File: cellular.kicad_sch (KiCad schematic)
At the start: 50 parts, among them J301 Conn_Coaxial, J302 Conn_Coaxial, J304 SIM8060-6-1-14-00-A, Q301 MMBT3904, Q302 MMBT3904, U301 BG95-M3, U302 SN74AXC4T245QPWRQ1, U303 SN74AXC4T245QPWRQ1

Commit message: hierarchy
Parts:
- renumbered C315 to C70, C325 to C71, C316 to C72, C326 to C73, C304 to C74, C305 to C75, C320 to C76, C301 to C77, C319 to C78, C318 to C79, C306 to C80, C302 to C81, C317 to C82, C307 to C83, C303 to C84, C308 to C85, C309 to C86, C310 to C87, D305 to D5, D304 to D6, D303 to D7, D302 to D8, FB301 to FB1, J304 to J5, J301 to J6, J302 to J7, Q302 to Q6, Q301 to Q7, R305 to R59, R303 to R60, R306 to R61, R304 to R62, R309 to R63, R310 to R64, R308 to R65, R312 to R66, R302 to R67, R311 to R68, R301 to R69, TP302 to TP18, TP303 to TP19, TP304 to TP20, TP305 to TP21, TP306 to TP22, TP307 to TP23, TP308 to TP24, TP301 to TP25, U302 to U24, U303 to U25, U301 to U26

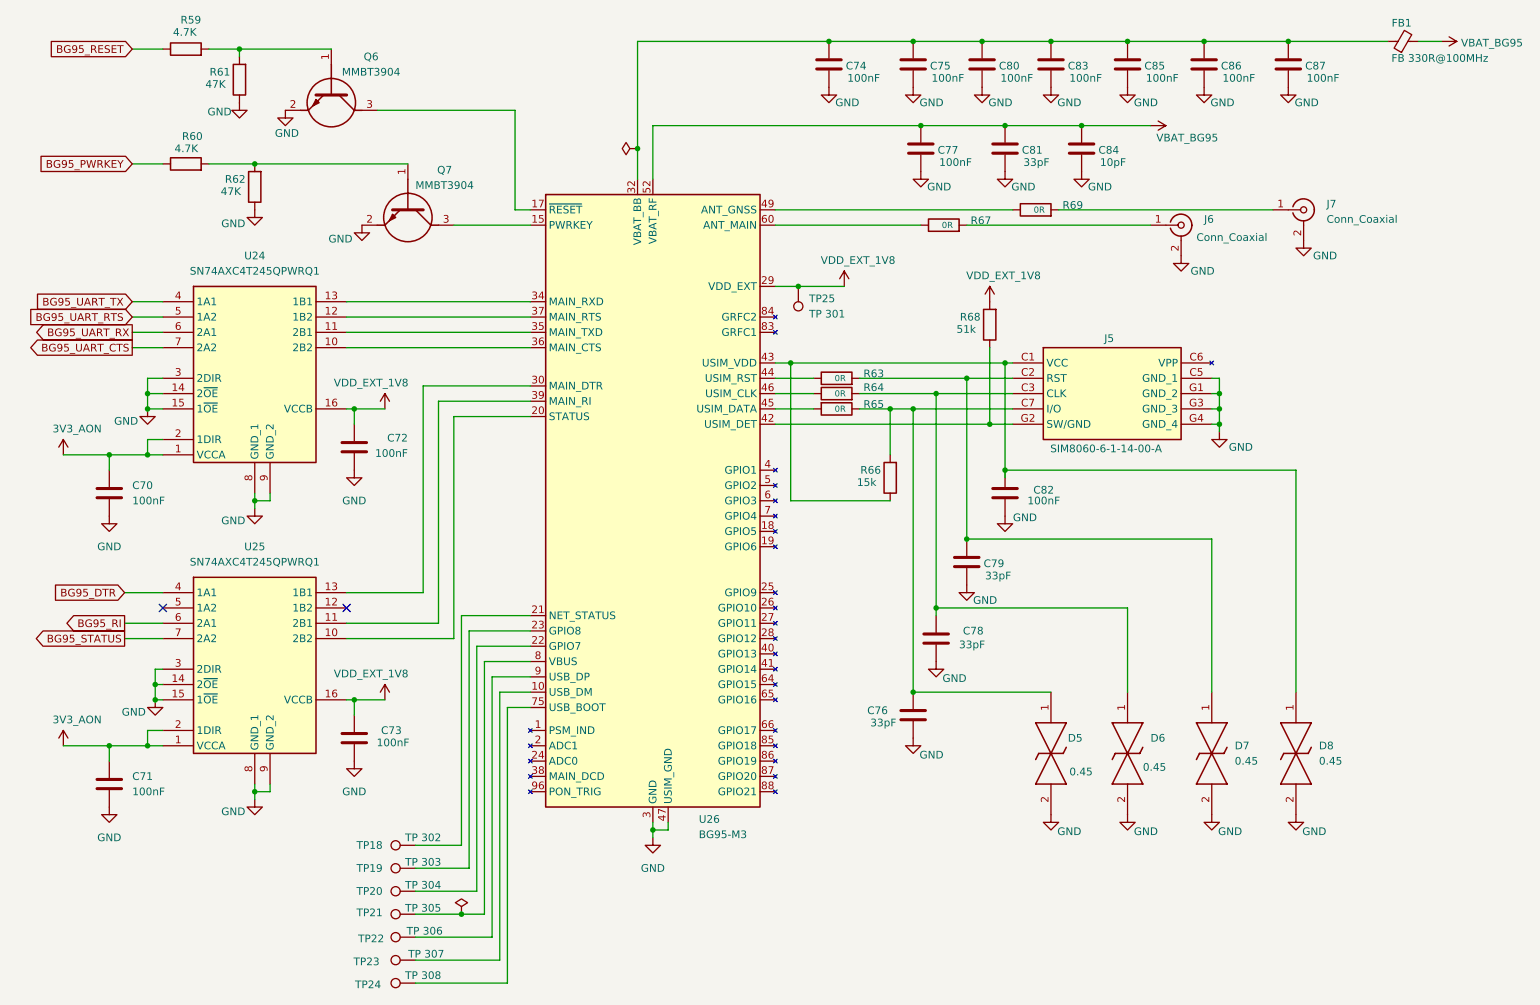
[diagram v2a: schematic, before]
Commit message: Fix SD card net and designator cleanup
This commit renumbers a few schematic components and fixes the SD-card interface wiring in the MCU and cellular sheets. It updates the DAT1/DAT2 pin directions and net labels, adds the missing power/junction connections for the SD rail, and aligns pull-up resistors and capacitor values with the revised SD_VDD routing. Related KiCad designator and power-symbol cleanup was also applied to keep the schematic consistent.
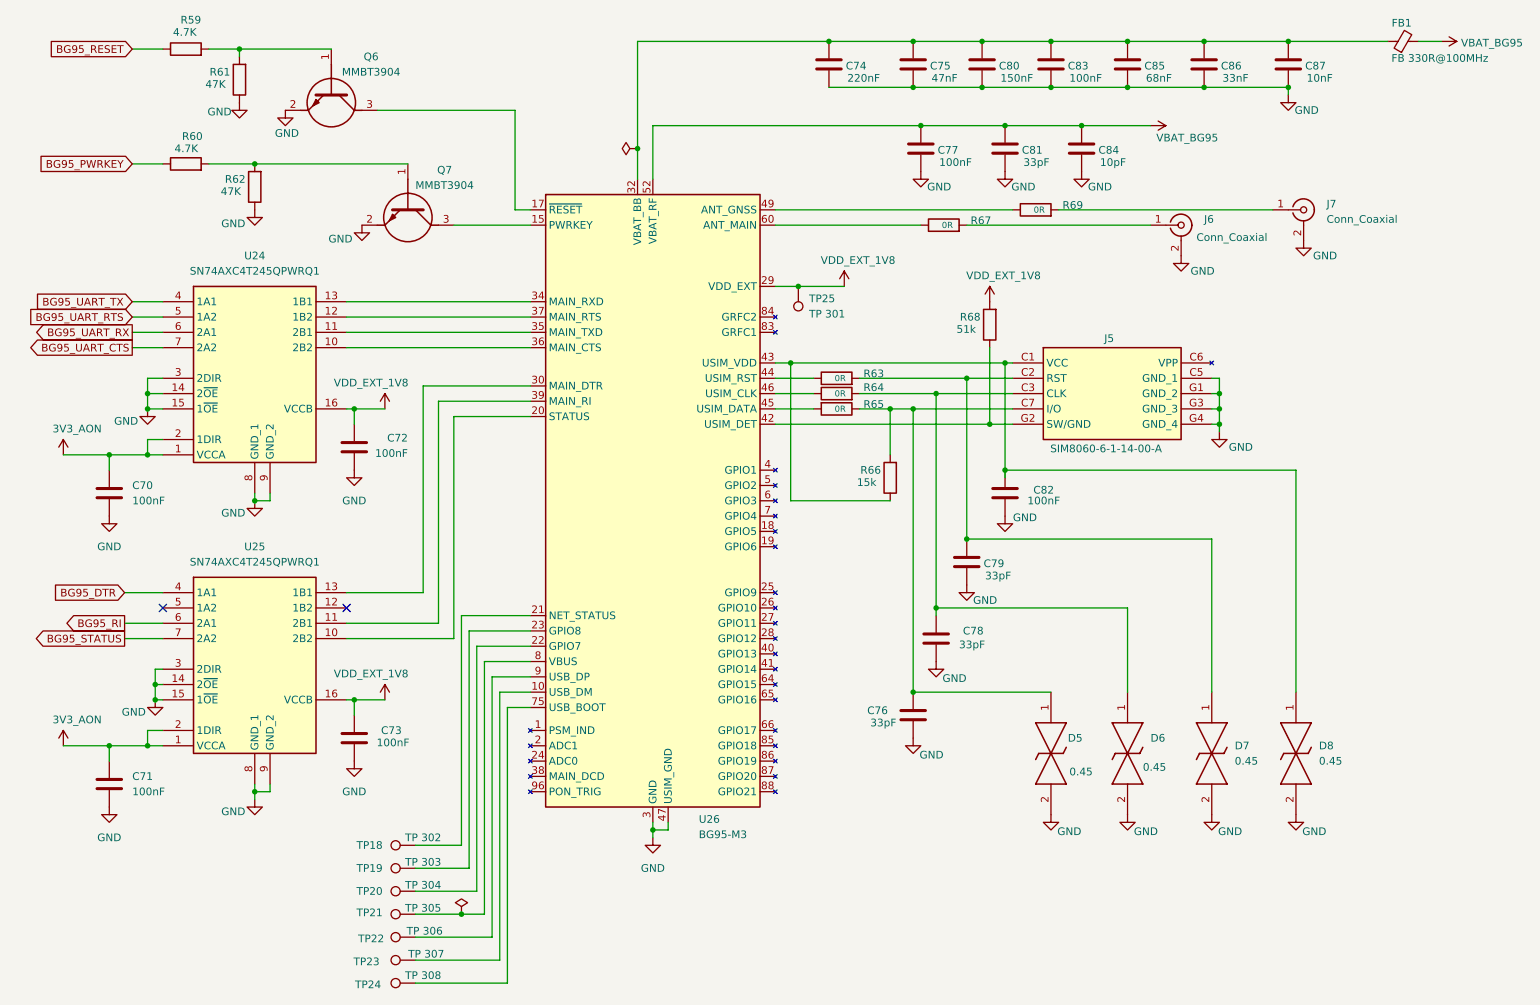
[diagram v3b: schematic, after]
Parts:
- C74: value 100nF -> 220nF
- C75: value 100nF -> 47nF
- C80: value 100nF -> 150nF
- C85: value 100nF -> 68nF
- C86: value 100nF -> 33nF
- C87: value 100nF -> 10nF

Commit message: Fix MCU net labels and passive values
This schematic update corrects a mislabeled power net from VSYS to 3V3_AON and fixes several capacitor values in the cellular path from nF to pF. It also reworks the MCU peripheral net/junction layout and adds the associated resistor references to match the intended signal routing and designators.
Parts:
- C80: value 150nF -> 150pF
- C83: value 100nF -> 100pF
- C85: value 68nF -> 68pF
- C86: value 33nF -> 33pF
- C87: value 10nF -> 10pF
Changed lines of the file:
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@@
 			)
 		)
-		(property "Value" "100nF"
+		(property "Value" "100pF"
 			(at 202.438 26.416 0)
 			(show_name no)
@@
 			)
 		)
-		(property "Value" "150nF"
+		(property "Value" "150pF"
 			(at 191.008 26.416 0)
 			(show_name no)
@@
 			)
 		)
-		(property "Value" "68nF"
+		(property "Value" "68pF"
 			(at 215.138 26.416 0)
 			(show_name no)
@@
 			)
 		)
-		(property "Value" "10nF"
+		(property "Value" "10pF"
 			(at 241.808 26.416 0)
 			(show_name no)
@@
 			)
 		)
-		(property "Value" "33nF"
+		(property "Value" "33pF"
 			(at 227.838 26.416 0)
 			(show_name no)

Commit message: bug fix
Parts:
- added C312, C313, C314, C315: DNP, RF_Module:ESP32-C6-MINI-1, symbol Device:C
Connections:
- net GND: now also C312.1, C313.1, C314.1, C315.1
- net at R69.1, U26.49 (ANT_GNSS): now also C312.2
- net at R67.1, U26.60 (ANT_MAIN): now also C314.2
- net at J6.1 (In), R67.2: now also C315.2
- net at J7.1 (In), R69.2: now also C313.2
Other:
- moved on the sheet: J6, J7, R67, R69

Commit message: Footprint
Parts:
- FB1: footprint (none) -> Inductor_SMD:L_0402_1005Metric
- J5: footprint SIM8060611400A -> SamacSys_Parts:SIM8060611400A
- J6, J7: footprint (none) -> Connector_Coaxial:U.FL_Hirose_U.FL-R-SMT-1_Vertical
- Q6, Q7: footprint SOT95P230X110-3N -> SamacSys_Parts:SOT95P230X110-3N
- R59, R60, R61, R62, R63, R64, R65, R66, R67, R68, R69: footprint (none) -> Resistor_SMD:R_0402_1005Metric
- TP18, TP19, TP20, TP21, TP22, TP23, TP24, TP25: footprint SOT95P230X110-3N -> TestPoint:TestPoint_Pad_D1.5mm
- U24, U25: footprint SOP65P640X120-16N -> SamacSys_Parts:SOP65P640X120-16N
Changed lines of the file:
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@@
 			)
 		)
-		(property "Footprint" "SOP65P640X120-16N"
+		(property "Footprint" "SamacSys_Parts:SOP65P640X120-16N"
 			(at 78.74 206.68 0)
 			(hide yes)
@@
 			)
 		)
-		(property "Footprint" ""
+		(property "Footprint" "Resistor_SMD:R_0402_1005Metric"
 			(at 163.83 80.518 90)
 			(hide yes)
@@
 			)
 		)
-		(property "Footprint" "SOT95P230X110-3N"
+		(property "Footprint" "SamacSys_Parts:SOT95P230X110-3N"
 			(at -8.56 54.61 0)
 			(hide yes)
@@
 			)
 		)
-		(property "Footprint" "SOT95P230X110-3N"
+		(property "Footprint" "SamacSys_Parts:SOT95P230X110-3N"
 			(at -21.26 35.56 0)
 			(hide yes)
@@
 			)
 		)
-		(property "Footprint" "SOT95P230X110-3N"
+		(property "Footprint" "TestPoint:TestPoint_Pad_D1.5mm"
 			(at 93.98 160.02 0)
 			(hide yes)
@@
 			)
 		)
-		(property "Footprint" ""
+		(property "Footprint" "Resistor_SMD:R_0402_1005Metric"
 			(at 66.548 26.67 90)
 			(hide yes)
@@
 			)
 		)
-		(property "Footprint" ""
+		(property "Footprint" "Inductor_SMD:L_0402_1005Metric"
 			(at 257.81 22.098 90)
 			(hide yes)
@@
 			)
 		)
-		(property "Footprint" ""
+		(property "Footprint" "Resistor_SMD:R_0402_1005Metric"
 			(at 163.83 79.502 90)
 			(hide yes)
@@
 			)
 		)
-		(property "Footprint" "SOT95P230X110-3N"
+		(property "Footprint" "TestPoint:TestPoint_Pad_D1.5mm"
 			(at 93.98 163.83 0)
 			(hide yes)
@@
 			)
 		)
-		(property "Footprint" "SIM8060611400A"
+		(property "Footprint" "SamacSys_Parts:SIM8060611400A"
 			(at 222.25 168.58 0)
 			(hide yes)
@@
 			)
 		)
-		(property "Footprint" "SOT95P230X110-3N"
+		(property "Footprint" "TestPoint:TestPoint_Pad_D1.5mm"
 			(at 152.4 60.96 0)
 			(hide yes)
@@
 			)
 		)
-		(property "Footprint" ""
+		(property "Footprint" "Resistor_SMD:R_0402_1005Metric"
 			(at 191.008 67.31 90)
 			(hide yes)
@@
 			)
 		)
-		(property "Footprint" "SOT95P230X110-3N"
+		(property "Footprint" "TestPoint:TestPoint_Pad_D1.5mm"
 			(at 93.98 148.59 0)
 			(hide yes)
@@
 			)
 		)
-		(property "Footprint" ""
+		(property "Footprint" "Resistor_SMD:R_0402_1005Metric"
 			(at 55.88 23.368 90)
 			(hide yes)
@@
 			)
 		)
-		(property "Footprint" "SOP65P640X120-16N"
+		(property "Footprint" "SamacSys_Parts:SOP65P640X120-16N"
 			(at 78.74 158.42 0)
 			(hide yes)
@@
 			)
 		)
-		(property "Footprint" ""
+		(property "Footprint" "Connector_Coaxial:U.FL_Hirose_U.FL-R-SMT-1_Vertical"
 			(at 238.76 50.8 0)
 			(hide yes)
@@
 			)
 		)
-		(property "Footprint" ""
+		(property "Footprint" "Resistor_SMD:R_0402_1005Metric"
 			(at 213.36 52.578 90)
 			(hide yes)
@@
 			)
 		)
-		(property "Footprint" ""
+		(property "Footprint" "Resistor_SMD:R_0402_1005Metric"
 			(at 55.88 42.418 90)
 			(hide yes)
@@
 			)
 		)
-		(property "Footprint" "SOT95P230X110-3N"
+		(property "Footprint" "TestPoint:TestPoint_Pad_D1.5mm"
 			(at 93.98 156.21 0)
 			(hide yes)
@@
 			)
 		)
-		(property "Footprint" ""
+		(property "Footprint" "Connector_Coaxial:U.FL_Hirose_U.FL-R-SMT-1_Vertical"
 			(at 259.08 48.26 0)
 			(hide yes)
@@
 			)
 		)
-		(property "Footprint" ""
+		(property "Footprint" "Resistor_SMD:R_0402_1005Metric"
 			(at 165.1 50.038 90)
 			(hide yes)
@@
 			)
 		)
-		(property "Footprint" ""
+		(property "Footprint" "Resistor_SMD:R_0402_1005Metric"
 			(at 174.498 92.71 90)
 			(hide yes)
@@
 			)
 		)
-		(property "Footprint" "SOT95P230X110-3N"
+		(property "Footprint" "TestPoint:TestPoint_Pad_D1.5mm"
 			(at 93.98 152.4 0)
 			(hide yes)
@@
 			)
 		)
-		(property "Footprint" ""
+		(property "Footprint" "Resistor_SMD:R_0402_1005Metric"
 			(at 163.83 77.978 90)
 			(hide yes)
@@
 			)
 		)
-		(property "Footprint" "SOT95P230X110-3N"
+		(property "Footprint" "TestPoint:TestPoint_Pad_D1.5mm"
 			(at 93.98 171.45 0)
 			(hide yes)
@@
 			)
 		)
-		(property "Footprint" "SOT95P230X110-3N"
+		(property "Footprint" "TestPoint:TestPoint_Pad_D1.5mm"
 			(at 93.98 167.64 0)
 			(hide yes)
@@
 			)
 		)
-		(property "Footprint" ""
+		(property "Footprint" "Resistor_SMD:R_0402_1005Metric"
 			(at 69.088 44.45 90)
 			(hide yes)

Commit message: Footprint
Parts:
- C312, C313, C314, C315, C70, C71, C72, C73, C74, C75, C76, C77, C78, C79, C80, C81, C82, C83, C84, C85, C86, C87: footprint RF_Module:ESP32-C6-MINI-1 -> Capacitor_SMD:C_0402_1005Metric
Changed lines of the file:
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@@
 			)
 		)
-		(property "Footprint" "RF_Module:ESP32-C6-MINI-1"
+		(property "Footprint" "Capacitor_SMD:C_0402_1005Metric"
 			(at 159.7152 48.26 0)
 			(hide yes)
@@
 			)
 		)
-		(property "Footprint" "RF_Module:ESP32-C6-MINI-1"
+		(property "Footprint" "Capacitor_SMD:C_0402_1005Metric"
 			(at 178.7652 34.29 0)
 			(hide yes)
@@
 			)
 		)
-		(property "Footprint" "RF_Module:ESP32-C6-MINI-1"
+		(property "Footprint" "Capacitor_SMD:C_0402_1005Metric"
 			(at 192.7352 34.29 0)
 			(hide yes)
@@
 			)
 		)
-		(property "Footprint" "RF_Module:ESP32-C6-MINI-1"
+		(property "Footprint" "Capacitor_SMD:C_0402_1005Metric"
 			(at 200.3552 20.32 0)
 			(hide yes)
@@
 			)
 		)
-		(property "Footprint" "RF_Module:ESP32-C6-MINI-1"
+		(property "Footprint" "Capacitor_SMD:C_0402_1005Metric"
 			(at 177.4952 20.32 0)
 			(hide yes)
@@
 			)
 		)
-		(property "Footprint" "RF_Module:ESP32-C6-MINI-1"
+		(property "Footprint" "Capacitor_SMD:C_0402_1005Metric"
 			(at 172.4152 48.26 0)
 			(hide yes)
@@
 			)
 		)
-		(property "Footprint" "RF_Module:ESP32-C6-MINI-1"
+		(property "Footprint" "Capacitor_SMD:C_0402_1005Metric"
 			(at 44.1452 147.32 0)
 			(hide yes)
@@
 			)
 		)
-		(property "Footprint" "RF_Module:ESP32-C6-MINI-1"
+		(property "Footprint" "Capacitor_SMD:C_0402_1005Metric"
 			(at 205.4352 34.29 0)
 			(hide yes)
@@
 			)
 		)
-		(property "Footprint" "RF_Module:ESP32-C6-MINI-1"
+		(property "Footprint" "Capacitor_SMD:C_0402_1005Metric"
 			(at 82.8548 91.44 0)
 			(hide yes)
@@
 			)
 		)
-		(property "Footprint" "RF_Module:ESP32-C6-MINI-1"
+		(property "Footprint" "Capacitor_SMD:C_0402_1005Metric"
 			(at 188.9252 20.32 0)
 			(hide yes)
@@
 			)
 		)
-		(property "Footprint" "RF_Module:ESP32-C6-MINI-1"
+		(property "Footprint" "Capacitor_SMD:C_0402_1005Metric"
 			(at 224.4852 50.8 0)
 			(hide yes)
@@
 			)
 		)
-		(property "Footprint" "RF_Module:ESP32-C6-MINI-1"
+		(property "Footprint" "Capacitor_SMD:C_0402_1005Metric"
 			(at 163.5252 20.32 0)
 			(hide yes)
@@
 			)
 		)
-		(property "Footprint" "RF_Module:ESP32-C6-MINI-1"
+		(property "Footprint" "Capacitor_SMD:C_0402_1005Metric"
 			(at 179.3748 123.19 0)
 			(hide yes)
@@
 			)
 		)
-		(property "Footprint" "RF_Module:ESP32-C6-MINI-1"
+		(property "Footprint" "Capacitor_SMD:C_0402_1005Metric"
 			(at 177.4952 128.27 0)
 			(hide yes)
@@
 			)
 		)
-		(property "Footprint" "RF_Module:ESP32-C6-MINI-1"
+		(property "Footprint" "Capacitor_SMD:C_0402_1005Metric"
 			(at 186.3852 102.87 0)
 			(hide yes)
@@
 			)
 		)
-		(property "Footprint" "RF_Module:ESP32-C6-MINI-1"
+		(property "Footprint" "Capacitor_SMD:C_0402_1005Metric"
 			(at 190.8048 99.06 0)
 			(hide yes)
@@
 			)
 		)
-		(property "Footprint" "RF_Module:ESP32-C6-MINI-1"
+		(property "Footprint" "Capacitor_SMD:C_0402_1005Metric"
 			(at 213.0552 20.32 0)
 			(hide yes)
@@
 			)
 		)
-		(property "Footprint" "RF_Module:ESP32-C6-MINI-1"
+		(property "Footprint" "Capacitor_SMD:C_0402_1005Metric"
 			(at 239.7252 20.32 0)
 			(hide yes)
@@
 			)
 		)
-		(property "Footprint" "RF_Module:ESP32-C6-MINI-1"
+		(property "Footprint" "Capacitor_SMD:C_0402_1005Metric"
 			(at 44.1452 99.06 0)
 			(hide yes)
@@
 			)
 		)
-		(property "Footprint" "RF_Module:ESP32-C6-MINI-1"
+		(property "Footprint" "Capacitor_SMD:C_0402_1005Metric"
 			(at 82.8548 139.7 0)
 			(hide yes)
@@
 			)
 		)
-		(property "Footprint" "RF_Module:ESP32-C6-MINI-1"
+		(property "Footprint" "Capacitor_SMD:C_0402_1005Metric"
 			(at 225.7552 20.32 0)
 			(hide yes)
@@
 			)
 		)
-		(property "Footprint" "RF_Module:ESP32-C6-MINI-1"
+		(property "Footprint" "Capacitor_SMD:C_0402_1005Metric"
 			(at 204.1652 50.8 0)
 			(hide yes)
